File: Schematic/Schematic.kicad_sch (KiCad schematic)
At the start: 8 parts, among them P1 RFID-RC522-MODULE, U1 RTC Clock

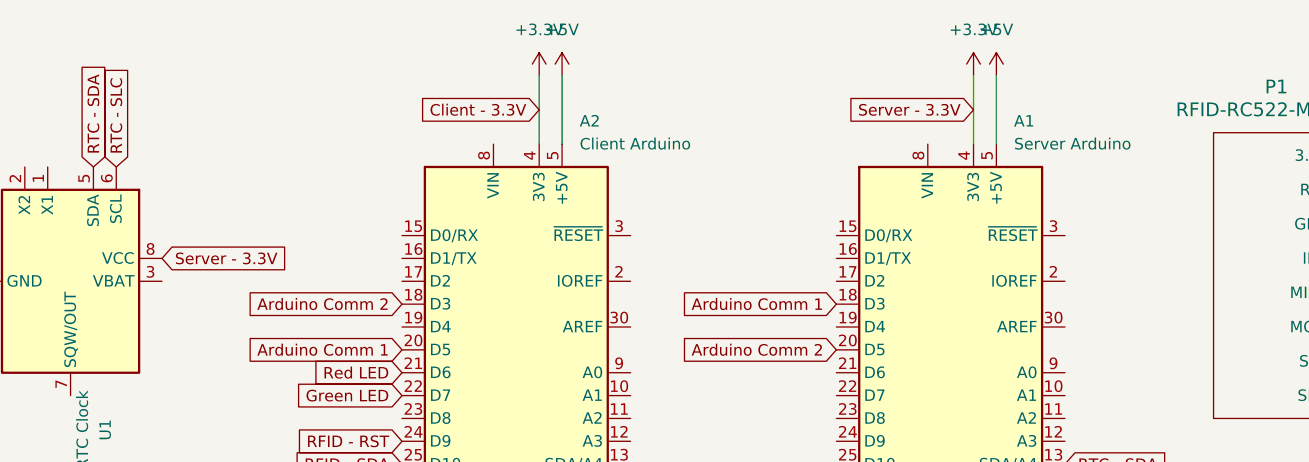
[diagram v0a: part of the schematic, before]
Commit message: Made the clock work
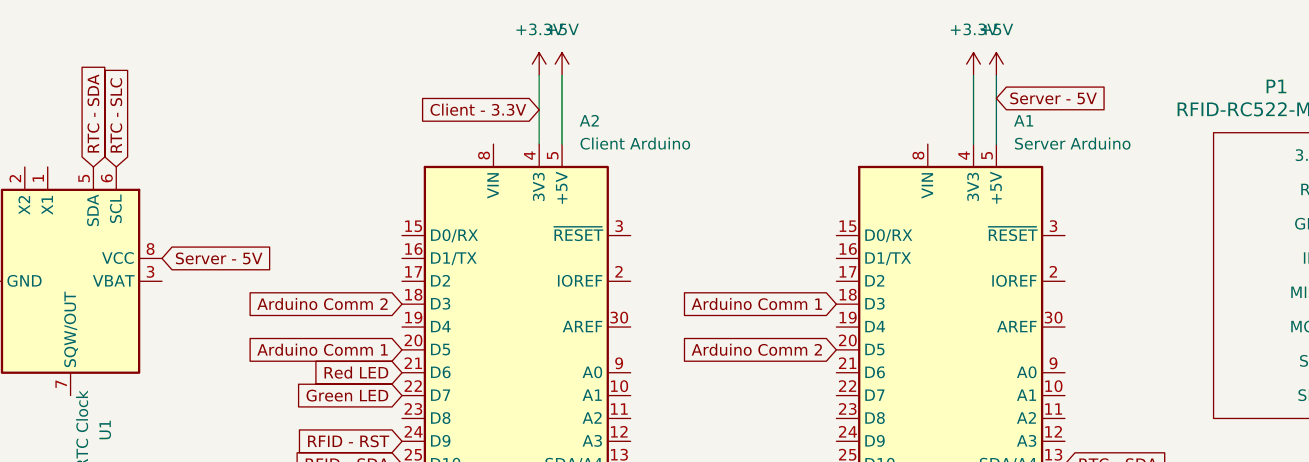
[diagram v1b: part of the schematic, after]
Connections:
- net +3.3V: no longer U1.8 (VCC)
- net +5V: now also U1.8 (VCC)
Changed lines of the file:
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@@
+    (stroke (width 0) (type default))
+  )
+  (wire (pts (xy 139.7 85.09) (xy 142.24 85.09))
+    (stroke (width 0) (type default))
+  )
+  (wire (pts (xy 93.98 85.09) (xy 93.98 87.63))
+    (stroke (width 0) (type default))
+  )
+  (wire (pts (xy 142.24 85.09) (xy 144.78 85.09))
+    (stroke (width 0) (type default))
+  )
+  (wire (pts (xy 91.44 85.09) (xy 93.98 85.09))
+    (stroke (width 0) (type default))
+  )
+  (wire (pts (xy 144.78 82.55) (xy 144.78 85.09))
+    (stroke (width 0) (type default))
+  )
+  (wire (pts (xy 34.29 68.58) (xy 34.29 73.66))
+    (stroke (width 0) (type default))
+  )
+  (wire (pts (xy 142.24 82.55) (xy 142.24 85.09))
+    (stroke (width 0) (type default))
+  )
+  (wire (pts (xy 96.52 21.59) (xy 96.52 29.21))
+    (stroke (width 0) (type default))
+  )
+  (wire (pts (xy 93.98 85.09) (xy 96.52 85.09))
+    (stroke (width 0) (type default))
+  )
+  (wire (pts (xy 96.52 82.55) (xy 96.52 85.09))
     (stroke (width 0) (type default))
   )
@@
     (stroke (width 0) (type default))
   )
-  (wire (pts (xy 139.7 85.09) (xy 142.24 85.09))
-    (stroke (width 0) (type default))
-  )
-  (wire (pts (xy 93.98 85.09) (xy 93.98 87.63))
-    (stroke (width 0) (type default))
-  )
-  (wire (pts (xy 142.24 85.09) (xy 144.78 85.09))
-    (stroke (width 0) (type default))
-  )
-  (wire (pts (xy 91.44 85.09) (xy 93.98 85.09))
-    (stroke (width 0) (type default))
-  )
-  (wire (pts (xy 144.78 82.55) (xy 144.78 85.09))
-    (stroke (width 0) (type default))
-  )
-  (wire (pts (xy 34.29 68.58) (xy 34.29 73.66))
-    (stroke (width 0) (type default))
-  )
-  (wire (pts (xy 142.24 82.55) (xy 142.24 85.09))
-    (stroke (width 0) (type default))
-  )
-  (wire (pts (xy 96.52 21.59) (xy 96.52 29.21))
-    (stroke (width 0) (type default))
-  )
-  (wire (pts (xy 93.98 85.09) (xy 96.52 85.09))
-    (stroke (width 0) (type default))
-  )
-  (wire (pts (xy 96.52 82.55) (xy 96.52 85.09))
-    (stroke (width 0) (type default))
-  )
   (wire (pts (xy 35.56 68.58) (xy 34.29 68.58))
     (stroke (width 0) (type default))
@@
     )
   )
-  (global_label "Server - 3.3V" (shape input) (at 144.78 25.4 180) (fields_autoplaced)
-    (effects (font (size 1.27 1.27)) (justify right))
-    (property "Intersheetrefs" "${INTERSHEET_REFS}" (at 128.3275 25.4 0)
-      (effects (font (size 1.27 1.27)) (justify right) hide)
+  (global_label "Server - 5V" (shape input) (at 147.32 24.13 0) (fields_autoplaced)
+    (effects (font (size 1.27 1.27)) (justify left))
+    (property "Intersheetrefs" "${INTERSHEET_REFS}" (at 161.9582 24.13 0)
+      (effects (font (size 1.27 1.27)) (justify left) hide)
     )
   )
@@
     )
   )
-  (global_label "Server - 3.3V" (shape input) (at 54.61 41.91 0) (fields_autoplaced)
-    (effects (font (size 1.27 1.27)) (justify left))
-    (property "Intersheetrefs" "${INTERSHEET_REFS}" (at 71.0625 41.91 0)
-      (effects (font (size 1.27 1.27)) (justify left) hide)
-    )
-  )
   (global_label "Client - GND" (shape input) (at 31.75 73.66 180) (fields_autoplaced)
     (effects (font (size 1.27 1.27)) (justify right))
@@
     )
   )
+  (global_label "Server - 5V" (shape input) (at 54.61 41.91 0) (fields_autoplaced)
+    (effects (font (size 1.27 1.27)) (justify left))
+    (property "Intersheetrefs" "${INTERSHEET_REFS}" (at 69.2482 41.91 0)
+      (effects (font (size 1.27 1.27)) (justify left) hide)
+    )
+  )

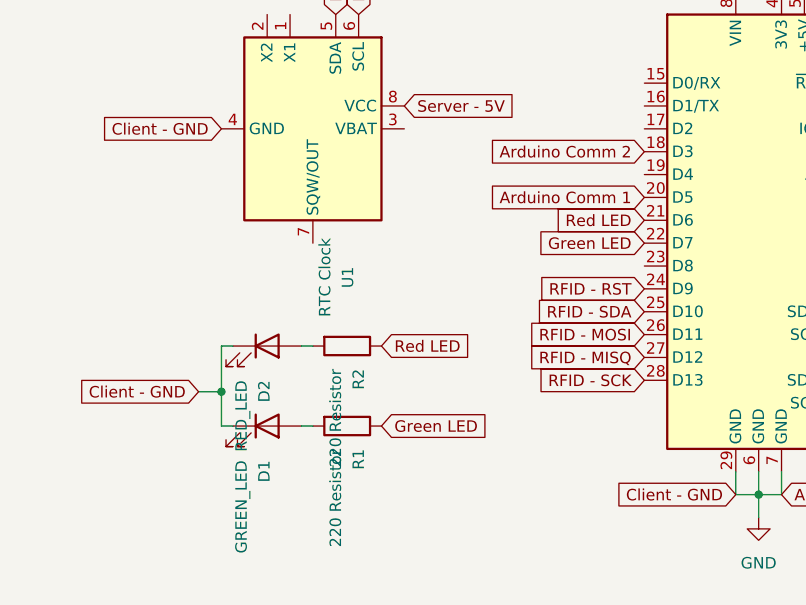
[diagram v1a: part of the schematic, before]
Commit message: Added blue LED
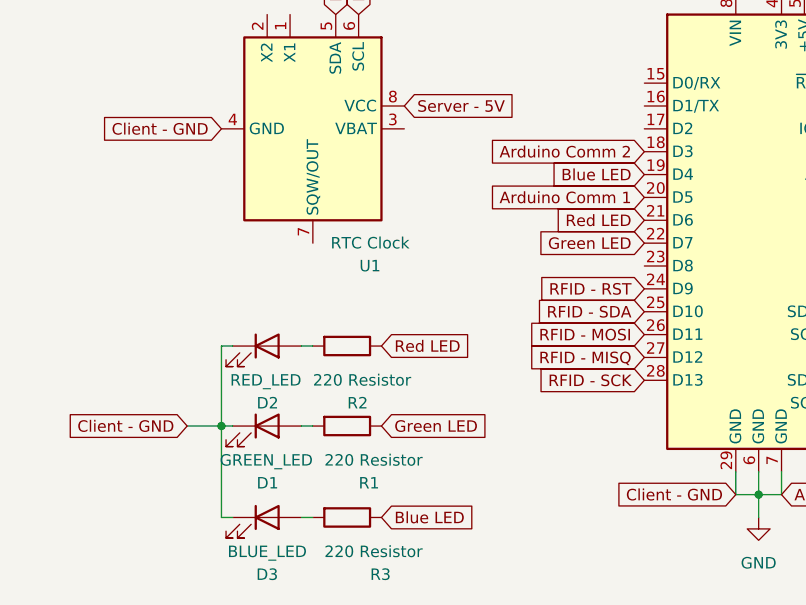
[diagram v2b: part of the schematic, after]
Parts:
- added D3: BLUE_LED, symbol Device:LED
- added R3: 220 Resistor, symbol Device:R
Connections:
- net GND: now also D3.1 (K)
- net Blue LED: now reaches A2.19 (D4)
- net Blue LED: now also R3.1
- new net: D3.2 (A), R3.2
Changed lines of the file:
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@@
   (junction (at 93.98 85.09) (diameter 0) (color 0 0 0 0)
   )
+  (junction (at 34.29 77.47) (diameter 0) (color 0 0 0 0)
+  )
   (junction (at 142.24 85.09) (diameter 0) (color 0 0 0 0)
   )
-  (junction (at 34.29 73.66) (diameter 0) (color 0 0 0 0)
-  )
   (wire (pts (xy 147.32 21.59) (xy 147.32 29.21))
     (stroke (width 0) (type default))
@@
     (stroke (width 0) (type default))
   )
+  (wire (pts (xy 34.29 77.47) (xy 34.29 87.63))
+    (stroke (width 0) (type default))
+  )
+  (wire (pts (xy 35.56 87.63) (xy 34.29 87.63))
+    (stroke (width 0) (type default))
+  )
   (wire (pts (xy 44.45 77.47) (xy 43.18 77.47))
     (stroke (width 0) (type default))
@@
     (stroke (width 0) (type default))
   )
+  (wire (pts (xy 34.29 68.58) (xy 34.29 77.47))
+    (stroke (width 0) (type default))
+  )
   (wire (pts (xy 139.7 82.55) (xy 139.7 85.09))
     (stroke (width 0) (type default))
@@
     (stroke (width 0) (type default))
   )
+  (wire (pts (xy 44.45 87.63) (xy 43.18 87.63))
+    (stroke (width 0) (type default))
+  )
   (wire (pts (xy 142.24 85.09) (xy 144.78 85.09))
     (stroke (width 0) (type default))
@@
     (stroke (width 0) (type default))
   )
-  (wire (pts (xy 34.29 68.58) (xy 34.29 73.66))
-    (stroke (width 0) (type default))
-  )
   (wire (pts (xy 142.24 82.55) (xy 142.24 85.09))
     (stroke (width 0) (type default))
@@
     (stroke (width 0) (type default))
   )
-  (wire (pts (xy 34.29 73.66) (xy 31.75 73.66))
-    (stroke (width 0) (type default))
-  )
-  (wire (pts (xy 34.29 77.47) (xy 34.29 73.66))
+  (wire (pts (xy 34.29 77.47) (xy 30.48 77.47))
     (stroke (width 0) (type default))
   )
@@
     )
   )
+  (global_label "Blue LED" (shape input) (at 52.07 87.63 0) (fields_autoplaced)
+    (effects (font (size 1.27 1.27)) (justify left))
+    (property "Intersheetrefs" "${INTERSHEET_REFS}" (at 63.5633 87.63 0)
+      (effects (font (size 1.27 1.27)) (justify left) hide)
+    )
+  )
   (global_label "RFID - RST" (shape input) (at 81.28 62.23 180) (fields_autoplaced)
     (effects (font (size 1.27 1.27)) (justify right))
@@
     )
   )
-  (global_label "Client - GND" (shape input) (at 31.75 73.66 180) (fields_autoplaced)
-    (effects (font (size 1.27 1.27)) (justify right))
-    (property "Intersheetrefs" "${INTERSHEET_REFS}" (at 15.9628 73.66 0)
+  (global_label "Client - GND" (shape input) (at 30.48 77.47 180) (fields_autoplaced)
+    (effects (font (size 1.27 1.27)) (justify right))
+    (property "Intersheetrefs" "${INTERSHEET_REFS}" (at 14.6928 77.47 0)
+      (effects (font (size 1.27 1.27)) (justify right) hide)
+    )
+  )
+  (global_label "Blue LED" (shape input) (at 81.28 49.53 180) (fields_autoplaced)
+    (effects (font (size 1.27 1.27)) (justify right))
+    (property "Intersheetrefs" "${INTERSHEET_REFS}" (at 69.7867 49.53 0)
       (effects (font (size 1.27 1.27)) (justify right) hide)
     )
@@
   (symbol (lib_id "Device:LED") (at 39.37 68.58 0) (unit 1)
     (in_bom yes) (on_board yes) (dnp no)
-    (property "Reference" "D2" (at 39.0525 72.39 90)
+    (property "Reference" "D2" (at 40.64 74.93 0)
       (effects (font (size 1.27 1.27)) (justify right))
     )
-    (property "Value" "RED_LED" (at 36.5125 72.39 90)
+    (property "Value" "RED_LED" (at 43.18 72.39 0)
       (effects (font (size 1.27 1.27)) (justify right))
     )
@@
     )
   )
+  (symbol (lib_id "Device:LED") (at 39.37 87.63 0) (unit 1)
+    (in_bom yes) (on_board yes) (dnp no)
+    (property "Reference" "D3" (at 39.37 93.98 0)
+      (effects (font (size 1.27 1.27)))
+    )
+    (property "Value" "BLUE_LED" (at 39.37 91.44 0)
+      (effects (font (size 1.27 1.27)))
+    )
+    (property "Footprint" "" (at 39.37 87.63 0)
+      (effects (font (size 1.27 1.27)) hide)
+    )
+    (property "Datasheet" "~" (at 39.37 87.63 0)
+      (effects (font (size 1.27 1.27)) hide)
+    )
+    (pin "1")
+    (pin "2")
+    (instances
+      (project "Schematic"
+        (path "/487fe9b8-9b70-479c-a0d2-f6fadf7e3c23"
+          (reference "D3") (unit 1)
+        )
+      )
+    )
+  )
   (symbol (lib_id "power:GND") (at 142.24 87.63 0) (unit 1)
     (in_bom yes) (on_board yes) (dnp no) (fields_autoplaced)
@@
         (path "/487fe9b8-9b70-479c-a0d2-f6fadf7e3c23"
           (reference "#PWR02") (unit 1)
+        )
+      )
+    )
+  )
+  (symbol (lib_id "Device:R") (at 48.26 87.63 270) (unit 1)
+    (in_bom yes) (on_board yes) (dnp no)
+    (property "Reference" "R3" (at 50.8 93.98 90)
+      (effects (font (size 1.27 1.27)) (justify left))
+    )
+    (property "Value" "220 Resistor" (at 45.72 91.44 90)
+      (effects (font (size 1.27 1.27)) (justify left))
+    )
+    (property "Footprint" "" (at 48.26 85.852 90)
+      (effects (font (size 1.27 1.27)) hide)
+    )
+    (property "Datasheet" "~" (at 48.26 87.63 0)
+      (effects (font (size 1.27 1.27)) hide)
+    )
+    (pin "1")
+    (pin "2")
+    (instances
+      (project "Schematic"
+        (path "/487fe9b8-9b70-479c-a0d2-f6fadf7e3c23"
+          (reference "R3") (unit 1)
         )
       )
@@
   )
   (symbol (lib_id "Device:LED") (at 39.37 77.47 0) (unit 1)
-    (in_bom yes) (on_board yes) (dnp no) (fields_autoplaced)
-    (property "Reference" "D1" (at 39.0525 81.28 90)
+    (in_bom yes) (on_board yes) (dnp no)
+    (property "Reference" "D1" (at 40.64 83.82 0)
       (effects (font (size 1.27 1.27)) (justify right))
     )
-    (property "Value" "GREEN_LED" (at 36.5125 81.28 90)
+    (property "Value" "GREEN_LED" (at 44.45 81.28 0)
       (effects (font (size 1.27 1.27)) (justify right))
     )
@@
   )
   (symbol (lib_id "Device:R") (at 48.26 77.47 270) (unit 1)
-    (in_bom yes) (on_board yes) (dnp no) (fields_autoplaced)
-    (property "Reference" "R1" (at 49.53 80.01 0)
-      (effects (font (size 1.27 1.27)) (justify left))
-    )
-    (property "Value" "220 Resistor" (at 46.99 80.01 0)
+    (in_bom yes) (on_board yes) (dnp no)
+    (property "Reference" "R1" (at 49.53 83.82 90)
+      (effects (font (size 1.27 1.27)) (justify left))
+    )
+    (property "Value" "220 Resistor" (at 45.72 81.28 90)
       (effects (font (size 1.27 1.27)) (justify left))
     )
@@
   )
   (symbol (lib_id "Timer_RTC:DS1307+") (at 44.45 44.45 270) (unit 1)
-    (in_bom yes) (on_board yes) (dnp no) (fields_autoplaced)
-    (property "Reference" "U1" (at 48.3361 60.96 0)
-      (effects (font (size 1.27 1.27)))
-    )
-    (property "Value" "RTC Clock" (at 45.7961 60.96 0)
+    (in_bom yes) (on_board yes) (dnp no)
+    (property "Reference" "U1" (at 50.8 59.69 90)
+      (effects (font (size 1.27 1.27)))
+    )
+    (property "Value" "RTC Clock" (at 50.8 57.15 90)
       (effects (font (size 1.27 1.27)))
     )
@@
   (symbol (lib_id "Device:R") (at 48.26 68.58 270) (unit 1)
     (in_bom yes) (on_board yes) (dnp no)
-    (property "Reference" "R2" (at 49.53 71.12 0)
-      (effects (font (size 1.27 1.27)) (justify left))
-    )
-    (property "Value" "220 Resistor" (at 46.99 71.12 0)
-      (effects (font (size 1.27 1.27)) (justify left))
-    )
+    (property "Reference" "R2" (at 48.26 74.93 90)
+      (effects (font (size 1.27 1.27)) (justify left))
+    )
+    (property "Value" "220 Resistor" (at 44.45 72.39 90)
+      (effects (font (size 1.27 1.27)) (justify left))
+    )
